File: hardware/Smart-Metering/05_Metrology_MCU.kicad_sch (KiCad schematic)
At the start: 0 parts

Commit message: Completa o esquemático: MCU, interface HMI e comunicações
05_Metrology_MCU: STM32F413RHT6 (símbolo oficial), mesma família da
plataforma de referência da biblioteca ADSW-PQ-CLS (NUCLEO-F413ZH).
SPI1 isolado para ADE9430/MCP3204, IRQ/DREADY/ZX em EXTI, CF1/CF2 em
timers, USART2 para a HMI, USART3 + DE para RS-485, USB FS, VBAT_SENSE,
estado do carregador, HSE 8 MHz, RTC com LSE 32,768 kHz e CR2032, SWD
de 10 pinos e LEDs de status e pulso.

07_HMI_Interface: conector J701 para a placa HMI (ESP32-P4), com +5V
protegido por PTC e UART/IRQ/EN com resistores de 33 Ω.

08_Communications: RS-485/Modbus isolada com ADM2587E (terminação por
jumper e TVS) e USB-C de serviço com CC de 5,1 kΩ, ESD USBLC6-2SC6 e
detecção de VBUS.

Gerador: direção dos labels pela orientação do pino, pinos empilhados
tratados como um ponto, flags de não conectado.
README e ARCHITECTURE atualizados com o estado completo.

Co-Authored-By: Claude Opus 5.5 <noreply@anthropic.com>
Claude-Session: https://claude.ai/code/session_012B8cVkhtjf3eg98UdpNCpf
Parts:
- added BT501: CR2032, Battery:BatteryHolder_Keystone_3034_1x20mm, symbol Device:Battery_Cell
- added C501, C502, C503, C504, C507, C509, C514: 100nF, Capacitor_SMD:C_0603_1608Metric, symbol SmartMetering:C_Vert
- added C505, C508: 4.7uF, Capacitor_SMD:C_0805_2012Metric, symbol SmartMetering:C_Vert
- added C506: 1uF, Capacitor_SMD:C_0603_1608Metric, symbol SmartMetering:C_Vert
- added C510, C511: 15pF, Capacitor_SMD:C_0603_1608Metric, symbol SmartMetering:C_Vert
- added C512, C513: 10pF, Capacitor_SMD:C_0603_1608Metric, symbol SmartMetering:C_Vert
- added D501: green, LED_SMD:LED_0603_1608Metric, symbol Device:LED
- added D502: red, LED_SMD:LED_0603_1608Metric, symbol Device:LED
- added FB501: 600R@100MHz, Inductor_SMD:L_0603_1608Metric, symbol SmartMetering:L_Horiz
- added J501: SWD, Connector_PinHeader_1.27mm:PinHeader_2x05_P1.27mm_Vertical, symbol Connector_Generic:Conn_02x05_Odd_Even
- added R501, R502: 10k, Resistor_SMD:R_0603_1608Metric, symbol SmartMetering:R_Vert
- added R503, R504: 1k, Resistor_SMD:R_0603_1608Metric, symbol SmartMetering:R_Vert
- added U501: STM32F413RHT6, Package_QFP:LQFP-64_10x10mm_P0.5mm, symbol MCU_ST_STM32F4:STM32F413RHTx
- added Y501: 8MHz, Crystal:Crystal_SMD_3225-4Pin_3.2x2.5mm, symbol Device:Crystal_GND24
- added Y502: 32.768kHz, Crystal:Crystal_SMD_3215-2Pin_3.2x1.5mm, symbol Device:Crystal
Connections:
- new net: D502.2 (A), R504.2
- new net: D501.2 (A), R503.2
- new net +3V3: C501.1, C502.1, C503.1, C504.1, C505.1, FB501.1, J501.1 (Pin_1), U501.19 (VDD), U501.32 (VDD), U501.48 (VDD), U501.64 (VDD)
- new net BOOT0: R501.1, U501.60 (BOOT0)
- new net BOOT1: R502.1, U501.28 (PB2)
- new net CHG_N: U501.9 (PC1)
- new net GND_SYS: BT501.2 (-), C501.2, C502.2, C503.2, C504.2, C505.2, C506.2, C507.2, C508.2, C509.2, C510.2, C511.2, C512.2, C513.2, C514.2, D501.1 (K), D502.1 (K), J501.3 (Pin_3), J501.5 (Pin_5), J501.9 (Pin_9), R501.2, R502.2, U501.12 (VSSA), U501.18 (VSS), U501.31 (VSS), U501.47 (VSS), U501.63 (VSS), Y501.2 (G), Y501.4 (G)
- new net HMI_EN: U501.40 (PC9)
- new net HMI_IRQ: U501.39 (PC8)
- new net HMI_RX: U501.17 (PA3)
- new net HMI_TX: U501.16 (PA2)
- new net HSE_IN: C510.1, U501.5 (PH0), Y501.1
- new net HSE_OUT: C511.1, U501.6 (PH1), Y501.3
- new net LED_PULSE: R504.1, U501.57 (PB5)
- new net LED_STAT: R503.1, U501.56 (PB4)
- new net LSE_IN: C512.1, U501.3 (PC14), Y502.1
- new net LSE_OUT: C513.1, U501.4 (PC15), Y502.2
- new net MCU_CF1: U501.14 (PA0)
- new net MCU_CF2: U501.15 (PA1)
- new net MCU_DREADY: U501.37 (PC6)
- new net MCU_IRQ0: U501.24 (PC4)
- new net MCU_IRQ1: U501.25 (PC5)
- new net MCU_MISO: U501.22 (PA6)
- new net MCU_MOSI: U501.23 (PA7)
- new net MCU_RESET_ADE: U501.27 (PB1)
- new net MCU_SCLK: U501.21 (PA5)
- new net MCU_SS_ADE: U501.20 (PA4)
- new net MCU_SS_SID: U501.26 (PB0)
- new net MCU_ZX: U501.38 (PC7)
- new net NRST: C509.1, J501.10 (Pin_10), U501.7 (NRST)
- new net PGOOD_N: U501.10 (PC2)
- new net RS485_DE: U501.53 (PC12)
- new net RS485_RX: U501.52 (PC11)
- new net RS485_TX: U501.51 (PC10)
- new net SWCLK: J501.4 (Pin_4), U501.49 (PA14)
- new net SWDIO: J501.2 (Pin_2), U501.46 (PA13)
- new net SWO: J501.6 (Pin_6), U501.55 (PB3)
- new net USB_DM: U501.44 (PA11)
- new net USB_DP: U501.45 (PA12)
- new net USB_VBUS_SENSE: U501.42 (PA9)
- new net VBAT_RTC: BT501.1 (+), C514.1, U501.1 (VBAT)
- new net VBAT_SENSE: U501.8 (PC0)
- new net VCAP: C508.1, U501.30 (VCAP_1)
- new net VDDA: C506.1, C507.1, FB501.2, U501.13 (VDDA)
- no-connect marks 0 -> 17
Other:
- note added: "MCU DE METROLOGIA — STM32F413RHT6 Escolhido por ser da mesma família da plataforma de referência da biblioteca ADSW-PQ-CLS (IEC 61000-4-30 Classe S) da ADI: NUCLEO-F413ZH. SPI1 (PA4-PA7) -> ADE9430 via isolador (folha 06); SS_SID (PB0) -> MCP3204 IRQ0/IRQ1/DREADY/ZX (PC4-PC7): EXTI; ZX em TIM3_CH2 (captura de período) CF1/CF2 (PA0/PA1): TIM2_ETR/TIM5_CH2 (contagem de pulsos de energia) USART2 (PA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"
- company: (none) -> Smart-Metering
- title: (none) -> Metrology MCU - STM32F413

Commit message: Revisão completa do esquemático e correções
Verificação automática sobre o netlist global (215 componentes, 176 nets):
sem pinos soltos, sem nets de alimentação sem fonte, sem saídas em
conflito e isolação íntegra (terras só se encontram nas barreiras
PS101, PS601, U601, U602 e U801).

Correções:
- footprint do ADE9430 inexistente na biblioteca KiCad trocado por
  QFN-40 6x6 (tamanho do pad exposto a confirmar);
- MISO do ADE9430 como tri-state (barramento compartilhado com MCP3204);
- PS101 com símbolo e footprint oficiais do IRM-10-5 (o símbolo genérico
  tinha AC/L e AC/N trocados);
- PWR_FLAG em HV_DC, HV_RTN, VBAT_RTC, VDDA, GND_485 e VIN_CHG;
- footprints para fusíveis, varistores, indutores e chave de energia;
- polarização de fail-safe opcional no RS-485 (R807/R808, DNP);
- notas de layout (retorno do AC/DC) e de firmware (VBUS no PA9).

Relatório com revisão por folha, orçamento de potência e pendências em
docs/REVISAO_ESQUEMATICO.md.

Co-Authored-By: Claude Opus 5.5 <noreply@anthropic.com>
Claude-Session: https://claude.ai/code/session_012B8cVkhtjf3eg98UdpNCpf
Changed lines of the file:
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@@
 		(property "Intersheetrefs" "${INTERSHEET_REFS}" (at 50.8 208.28 0) (hide yes) (effects (font (size 1.27 1.27))))
+	)
+	(label "VBAT_RTC" (at 63.5 198.12 270)
+		(effects (font (size 1.27 1.27)) (justify right bottom))
+	)
+	(label "VDDA" (at 101.6 30.48 270)
+		(effects (font (size 1.27 1.27)) (justify right bottom))
 	)
 	(global_label "+3V3" (shape bidirectional) (at 259.08 58.42 180)
@@
 			)
 		)
+	)
+	(symbol
+		(lib_id "power:PWR_FLAG")
+		(at 63.5 198.12 0)
+		(unit 1)(body_style 1)
+		(exclude_from_sim no)(in_bom yes)(on_board yes)(in_pos_files yes)(dnp no)
+		(property "Reference" "#FLG501" (at 63.5 194.31 0) (effects (font (size 1.27 1.27))))
+		(property "Value" "PWR_FLAG" (at 63.5 195.58 0) (effects (font (size 1.27 1.27))))
+		(property "Footprint" "" (at 63.5 198.12 0) (effects (font (size 1.27 1.27)) (hide yes)))
+		(property "Datasheet" "" (at 63.5 198.12 0) (effects (font (size 1.27 1.27)) (hide yes)))
+		(property "Description" "" (at 63.5 198.12 0) (effects (font (size 1.27 1.27)) (hide yes)))
+		(pin "1")
+		(instances
+			(project "Smart-Metering"
+				(path "/5fa62d70-4279-48bb-8603-6bcc60fb353a/a10e1005-0005-4e05-9005-000000000005" (reference "#FLG501") (unit 1))
+			)
+		)
+	)
+	(symbol
+		(lib_id "power:PWR_FLAG")
+		(at 101.6 30.48 0)
+		(unit 1)(body_style 1)
+		(exclude_from_sim no)(in_bom yes)(on_board yes)(in_pos_files yes)(dnp no)
+		(property "Reference" "#FLG502" (at 101.6 26.67 0) (effects (font (size 1.27 1.27))))
+		(property "Value" "PWR_FLAG" (at 101.6 27.94 0) (effects (font (size 1.27 1.27))))
+		(property "Footprint" "" (at 101.6 30.48 0) (effects (font (size 1.27 1.27)) (hide yes)))
+		(property "Datasheet" "" (at 101.6 30.48 0) (effects (font (size 1.27 1.27)) (hide yes)))
+		(property "Description" "" (at 101.6 30.48 0) (effects (font (size 1.27 1.27)) (hide yes)))
+		(pin "1")
+		(instances
+			(project "Smart-Metering"
+				(path "/5fa62d70-4279-48bb-8603-6bcc60fb353a/a10e1005-0005-4e05-9005-000000000005" (reference "#FLG502") (unit 1))
+			)
+		)

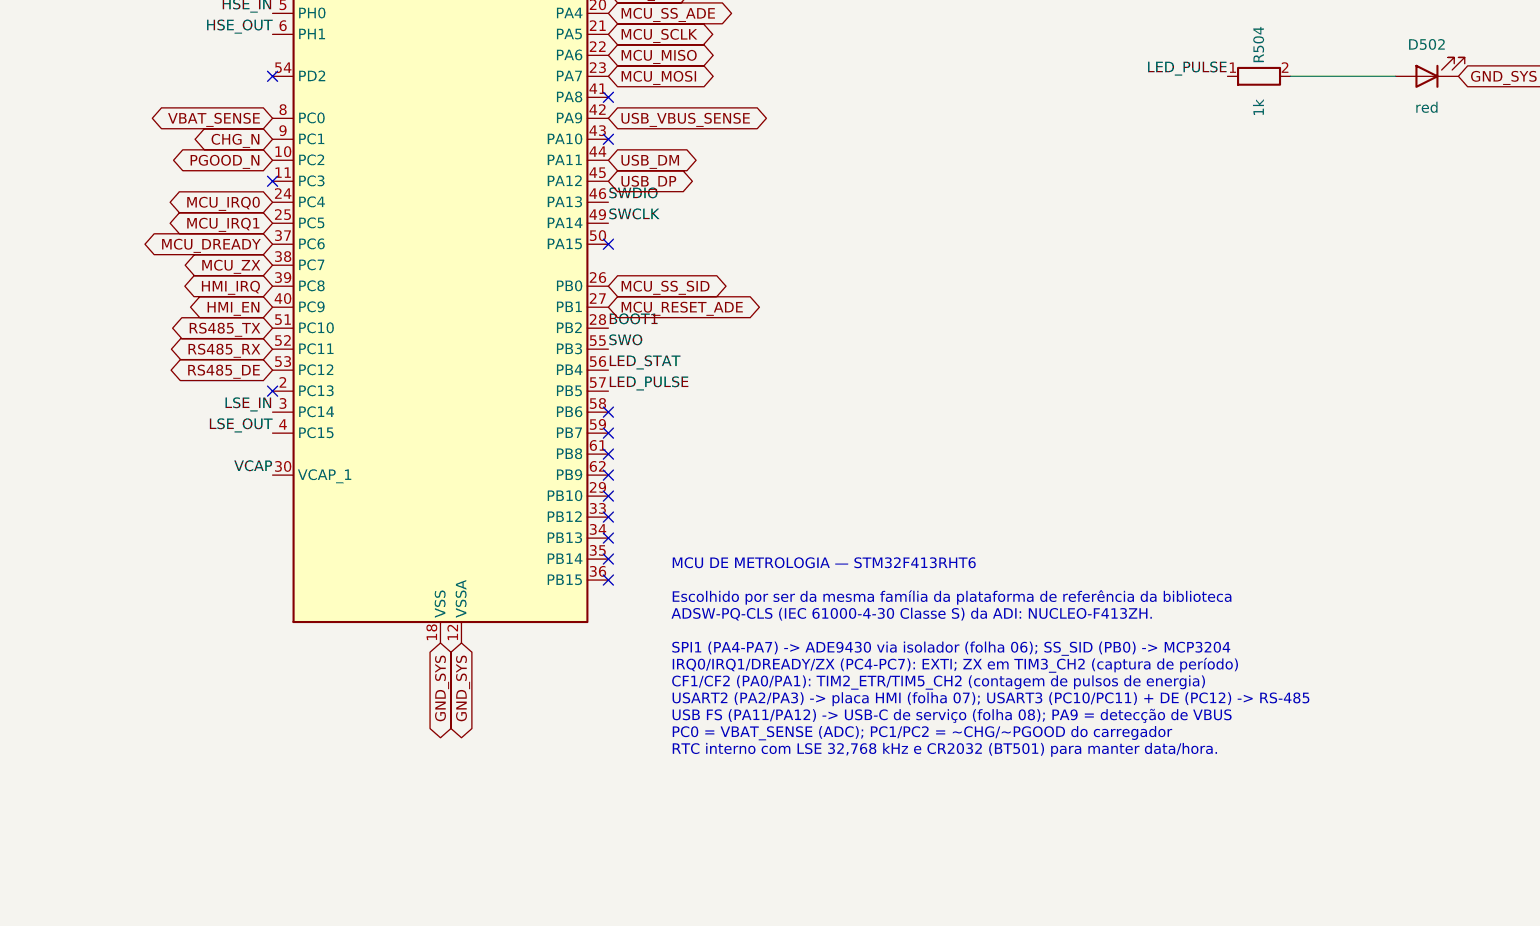
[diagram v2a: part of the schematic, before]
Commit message: Troca o carregador linear BQ24074 pelo chaveado BQ25895
O BQ24074 limitava a entrada a 1,48 A e, com o sistema consumindo cerca
de 5,2 W, sobravam só ~0,3 A para carregar a bateria (mais de 8 h).

09_Power_Supplies:
- U901 BQ25895RTW (símbolo oficial): carregador chaveado com power path
  NVDC; limite de entrada de 2,0 A por R902 (180 Ω), o máximo do
  IRM-10-5; carga de ~0,85 A com a tela ligada;
- D+/D- unidos para detecção como carregador dedicado (DCP);
- divisor do NTC a partir de REGN, L903 2,2 uH, bootstrap, REGN, PMID,
  SYS e BAT conforme o datasheet;
- I2C, ~INT e STAT para o MCU; D901/D902 passam a SS54 (SMC);
- PWR_FLAG em VSYS (pino SYS é passivo no símbolo oficial).

05_Metrology_MCU: PC2 = CHG_INT_N, PB6/PB7 = I2C1 para o carregador.
Documentação de revisão e README atualizados.

Co-Authored-By: Claude Opus 5.5 <noreply@anthropic.com>
Claude-Session: https://claude.ai/code/session_012B8cVkhtjf3eg98UdpNCpf
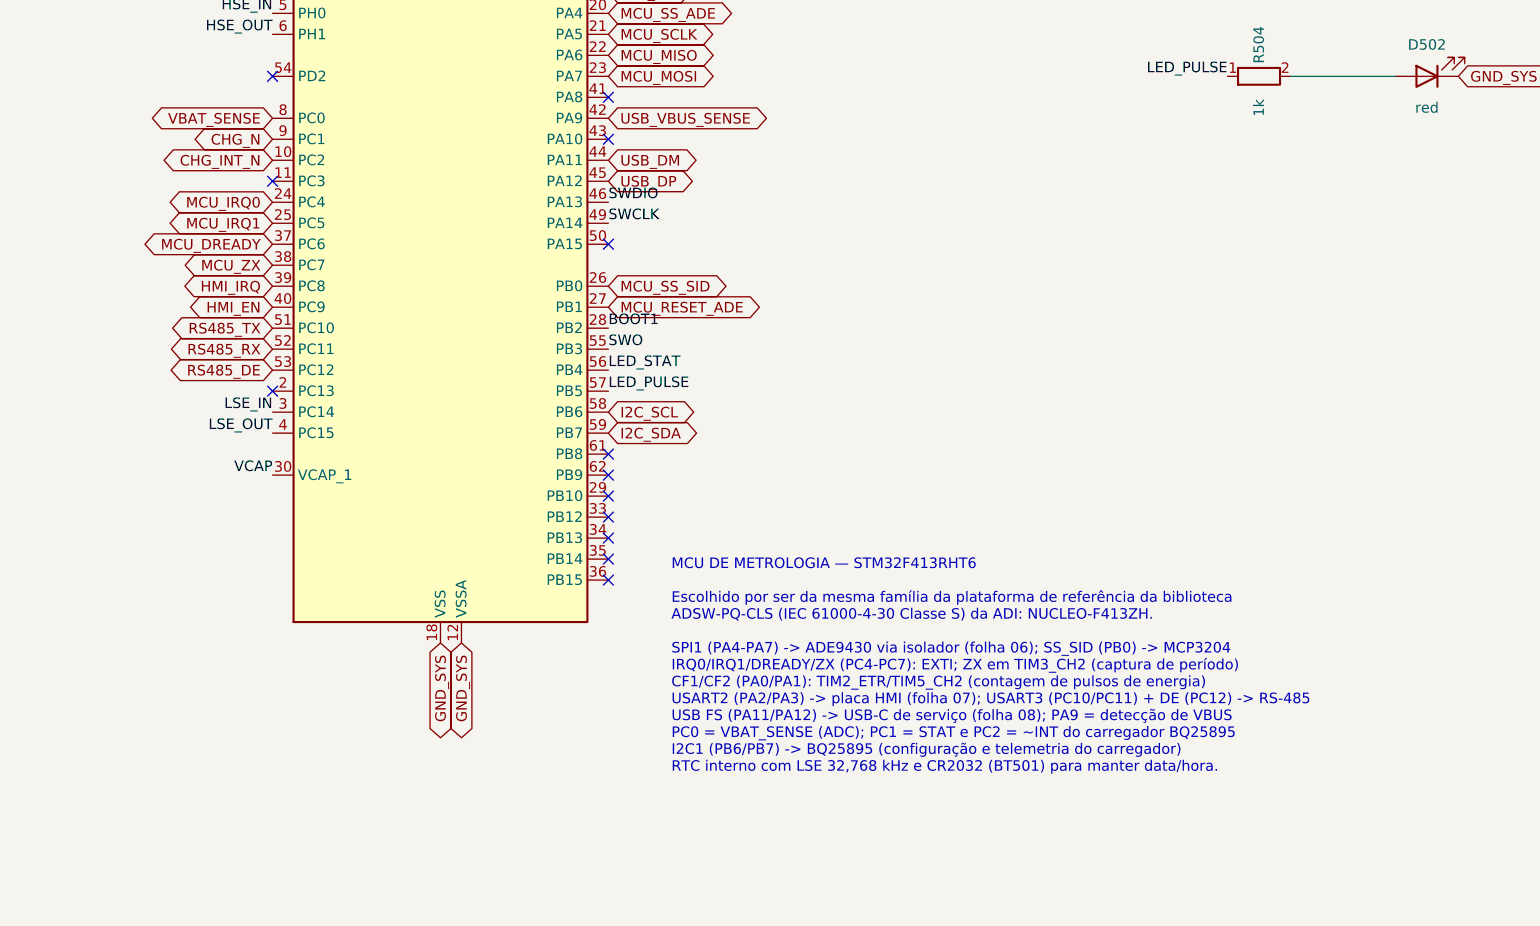
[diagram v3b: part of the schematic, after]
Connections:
- net I2C_SCL: now reaches U501.58 (PB6)
- net I2C_SDA: now reaches U501.59 (PB7)
- net PGOOD_N renamed CHG_INT_N
- no-connect marks 17 -> 15
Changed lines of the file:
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@@
 		(comment 2 "Platform matches the ADSW-PQ-CLS reference (NUCLEO-F413ZH)")
 	)
-	(text "MCU DE METROLOGIA — STM32F413RHT6\n\nEscolhido por ser da mesma família da plataforma de referência da biblioteca\nADSW-PQ-CLS (IEC 61000-4-30 Classe S) da ADI: NUCLEO-F413ZH.\n\nSPI1 (PA4-PA7) -> ADE9430 via isolador (folha 06); SS_SID (PB0) -> MCP3204\nIRQ0/IRQ1/DREADY/ZX (PC4-PC7): EXTI; ZX em TIM3_CH2 (captura de período)\nCF1/CF2 (PA0/PA1): TIM2_ETR/TIM5_CH2 (contagem de pulsos de energia)\nUSART2 (PA2/PA3) -> placa HMI (folha 07); USART3 (PC10/PC11) + DE (PC12) -> RS-485\nUSB FS (PA11/PA12) -> USB-C de serviço (folha 08); PA9 = detecção de VBUS\nPC0 = VBAT_SENSE (ADC); PC1/PC2 = ~CHG/~PGOOD do carregador\nRTC interno com LSE 32,768 kHz e CR2032 (BT501) para manter data/hora."
+	(text "MCU DE METROLOGIA — STM32F413RHT6\n\nEscolhido por ser da mesma família da plataforma de referência da biblioteca\nADSW-PQ-CLS (IEC 61000-4-30 Classe S) da ADI: NUCLEO-F413ZH.\n\nSPI1 (PA4-PA7) -> ADE9430 via isolador (folha 06); SS_SID (PB0) -> MCP3204\nIRQ0/IRQ1/DREADY/ZX (PC4-PC7): EXTI; ZX em TIM3_CH2 (captura de período)\nCF1/CF2 (PA0/PA1): TIM2_ETR/TIM5_CH2 (contagem de pulsos de energia)\nUSART2 (PA2/PA3) -> placa HMI (folha 07); USART3 (PC10/PC11) + DE (PC12) -> RS-485\nUSB FS (PA11/PA12) -> USB-C de serviço (folha 08); PA9 = detecção de VBUS\nPC0 = VBAT_SENSE (ADC); PC1 = STAT e PC2 = ~INT do carregador BQ25895\nI2C1 (PB6/PB7) -> BQ25895 (configuração e telemetria do carregador)\nRTC interno com LSE 32,768 kHz e CR2032 (BT501) para manter data/hora."
 		(exclude_from_sim no)(at 180.34 175.26 0)
 		(effects (font (size 1.27 1.27)) (justify left top))
@@
 	(no_connect (at 132.08 116.84)
 	)
-	(no_connect (at 172.72 157.48)
-	)
-	(no_connect (at 172.72 160.02)
-	)
 	(no_connect (at 172.72 162.56)
 	)
@@
 		(property "Intersheetrefs" "${INTERSHEET_REFS}" (at 132.08 124.46 0) (hide yes) (effects (font (size 1.27 1.27))))
 	)
-	(global_label "PGOOD_N" (shape bidirectional) (at 132.08 127 180)
+	(global_label "CHG_INT_N" (shape bidirectional) (at 132.08 127 180)
 		(effects (font (size 1.27 1.27)) (justify right))
 		(property "Intersheetrefs" "${INTERSHEET_REFS}" (at 132.08 127 0) (hide yes) (effects (font (size 1.27 1.27))))
@@
 		(effects (font (size 1.27 1.27)) (justify left bottom))
 	)
+	(global_label "I2C_SCL" (shape bidirectional) (at 172.72 157.48 0)
+		(effects (font (size 1.27 1.27)) (justify left))
+		(property "Intersheetrefs" "${INTERSHEET_REFS}" (at 172.72 157.48 0) (hide yes) (effects (font (size 1.27 1.27))))
+	)
+	(global_label "I2C_SDA" (shape bidirectional) (at 172.72 160.02 0)
+		(effects (font (size 1.27 1.27)) (justify left))
+		(property "Intersheetrefs" "${INTERSHEET_REFS}" (at 172.72 160.02 0) (hide yes) (effects (font (size 1.27 1.27))))
+	)
 	(label "BOOT0" (at 132.08 104.14 180)
